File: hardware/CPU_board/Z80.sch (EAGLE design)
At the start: 46 parts, among them IC11 74HCT245DW, IC3 ATF16V8BP3, IC6 74AC273N, IC9 74HCT138N

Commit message: CPU board update
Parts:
- removed C11: 100n, rcl:C-EUC0805
- removed C15, C21, C6: 100n, rcl:C-EUC1206
- added JP3: (no value), pinhead:PINHD-1X2
- added R14: 10k, rcl:R-EU_0204/7
- IC3: value ATF16V8BP3 -> (none); device atmel:ATF16V8BP3 -> pal:16V8
- R1, R8: device rcl:R-EU_0207/12 -> rcl:R-EU_0204/7
- R10: device rcl:R-EU_0204/7 -> rcl:R-EU_R0603
- R4: device rcl:R-EU_R1206 -> rcl:R-EU_R0603
- R9: device rcl:R-EU_0204/7 -> rcl:R-EU_0207/10
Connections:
- removed net CF_DELAYED_RD: CON1G$1./IORD
- removed net CF_DELAYED_WR: CON1G$1./IOWR
- removed net CS_1: IC9A.Y1, SV2.58
- net !IORQ: now also IC3G$1.I6; no longer IC3.I3
- net !MREQ: now also IC3G$1.I3; no longer IC3.CLK
- net !RESET: now also R14.1
- net A15: now also IC3G$1.I4; no longer IC3.I2
- net A4: now also IC3G$1.I1; no longer IC3.I6
- net CF_CS0: now also IC3G$1.O5
- net CLK: now also IC3G$1.CLK
- net CS_EPROM: now also IC3G$1.O1; no longer IC3.O3
- net CS_RAM1: now also IC3G$1.O7; no longer IC3.O1
- net CS_RAM2: now also IC3G$1.O6; no longer IC3.O2
- net DMA_CS: now also IC9A.Y1; no longer IC3.O6
- net GND: now also JP3.2, SV2.58; no longer C11.2, C15.2, C21.2, C6.2, IC3.GND
- net INTA: now also IC3G$1.O0; no longer IC3.O4
- net LOCAL_IO_CS: now also IC3G$1.I7; no longer IC3.I5
- net M1: now also IC3G$1.I0; no longer IC3.I4
- net PORT_CS: now also IC3G$1.O3; no longer IC3.O5
- net RD: now also CON1G$1./IORD
- net ROM_SHADOW: now also IC3G$1.I5; no longer IC3.I1
- net VCC: now also JP3.1, R14.2; no longer C11.1, C15.1, C21.1, C6.1, IC3.VCC
- net WR: now also CON1G$1./IOWR, IC3G$1.I2
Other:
- moved on the sheet: C12, C13, C14, C18, C22, C7, C9, IC1, R2, R3, R4, R5

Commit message: CPU board update
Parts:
- added C4: 100n, rcl:C-EUC0603
- added D1: 1N4148DO35-7, diode:1N4148DO35-7
- added JP1: (no value), pinhead:PINHD-1X2
- added R15: (no value), rcl:R-EU_R0603
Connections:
- new net N$2: JP1.2, R15.1
- net !RESET: now also C4.1, D1.A, R15.2
- net GND: now also C4.2, JP1.1
- net VCC: now also D1.C
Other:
- moved on the sheet: R14

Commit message: bugs in CPU board design fixed
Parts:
- removed R9: 10k, rcl:R-EU_0207/10
- added R16: (no value), rcl:R-EU_0204/5
- added R17: (no value), rcl:R-EU_R0603
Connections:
- removed net N$20: IC9A.G1, R9.1
- new net N$3: IC2.IEI, R16.1
- net M1: now also IC9A.G1
- net VCC: now also R16.2, R17.2; no longer R9.2
- net WAIT: now also R17.1
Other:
- moved on the sheet: IC1, R2, R3, R4, R5

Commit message: CPU board and I/O board update
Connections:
- net !IORQ: now also SV2.44
- net M1: now also SV2.43
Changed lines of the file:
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@@
 <pinref part="SV2" gate="1" pin="1"/>
 <wire x1="160.02" y1="-71.12" x2="165.1" y2="-71.12" width="0.1524" layer="91"/>
+<label x="165.1" y="-71.12" size="1.4224" layer="95" xref="yes"/>
 </segment>
 </net>
@@
 <label x="43.18" y="-109.22" size="1.4224" layer="95" rot="R180" xref="yes"/>
 </segment>
+<segment>
+<pinref part="SV2" gate="1" pin="44"/>
+<wire x1="144.78" y1="-17.78" x2="139.7" y2="-17.78" width="0.1524" layer="91"/>
+<label x="139.7" y="-17.78" size="1.4224" layer="95" rot="R180" xref="yes"/>
+</segment>
 </net>
 <net name="!MREQ" class="0">
@@
 <label x="114.3" y="-144.78" size="1.4224" layer="95" rot="R180" xref="yes"/>
 </segment>
-</net>
+<segment>
+<pinref part="SV2" gate="1" pin="43"/>
+<wire x1="160.02" y1="-17.78" x2="165.1" y2="-17.78" width="0.1524" layer="91"/>
+<label x="165.1" y="-17.78" size="1.4224" layer="95" xref="yes"/>
+</segment>
+</net>

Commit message: CPU and I/O board update
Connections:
- removed net 8275_DACK: SV2.2
- removed net RDYIN: SV2.1
- new net IEO: IC2.IEO, SV2.2
- net INT: now also IC2.INT/PLSE
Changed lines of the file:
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@@
 <junction x="-17.78" y="30.48"/>
+</segment>
+<segment>
+<pinref part="IC2" gate="G$1" pin="INT/PLSE"/>
+<wire x1="-88.9" y1="12.7" x2="-93.98" y2="12.7" width="0.1524" layer="91"/>
 </segment>
 </net>
@@
 </segment>
 </net>
-<net name="RDYIN" class="0">
-<segment>
-<pinref part="SV2" gate="1" pin="1"/>
-<wire x1="160.02" y1="-71.12" x2="165.1" y2="-71.12" width="0.1524" layer="91"/>
-<label x="165.1" y="-71.12" size="1.4224" layer="95" xref="yes"/>
-</segment>
-</net>
 <net name="!RESET" class="0">
 <segment>
@@
 </segment>
 </net>
-<net name="8275_DACK" class="0">
-<segment>
-<pinref part="SV2" gate="1" pin="2"/>
-<wire x1="144.78" y1="-71.12" x2="139.7" y2="-71.12" width="0.1524" layer="91"/>
-<label x="139.7" y="-71.12" size="1.4224" layer="95" rot="R180" xref="yes"/>
-</segment>
-</net>
 <net name="!IORQ" class="0">
 <segment>
@@
 </segment>
 </net>
+<net name="IEO" class="0">
+<segment>
+<pinref part="SV2" gate="1" pin="2"/>
+<wire x1="144.78" y1="-71.12" x2="139.7" y2="-71.12" width="0.1524" layer="91"/>
+<label x="139.7" y="-71.12" size="1.778" layer="95" rot="R180" xref="yes"/>
+</segment>
+<segment>
+<pinref part="IC2" gate="G$1" pin="IEO"/>
+<wire x1="-88.9" y1="7.62" x2="-93.98" y2="7.62" width="0.1524" layer="91"/>
+</segment>
+</net>

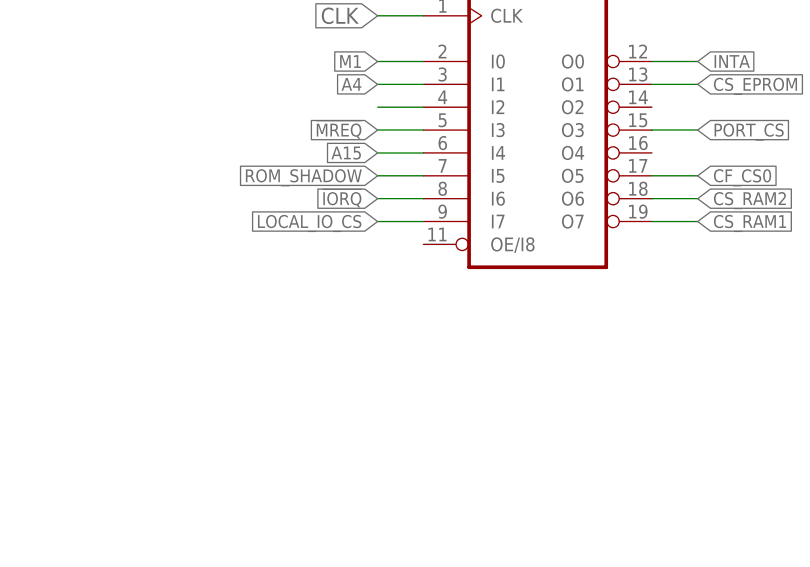
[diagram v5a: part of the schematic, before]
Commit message: Bug in CPU board fixed
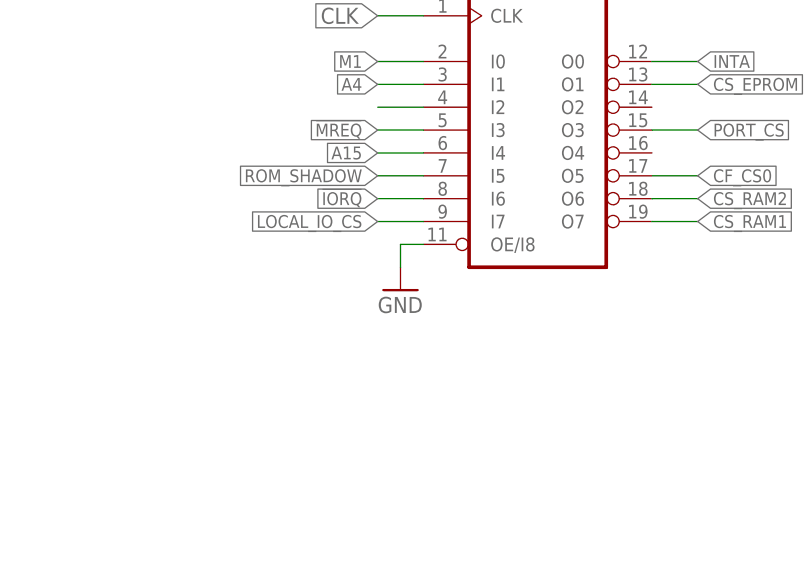
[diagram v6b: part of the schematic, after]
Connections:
- net GND: now also IC3G$1.OE/I8
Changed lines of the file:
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@@
 <part name="R16" library="rcl" deviceset="R-EU_" device="0204/5"/>
 <part name="R17" library="rcl" deviceset="R-EU_" device="R0603"/>
+<part name="GND10" library="supply1" deviceset="GND" device=""/>
 </parts>
 <sheets>
@@
 <instance part="R16" gate="G$1" x="-111.76" y="25.4" rot="R90"/>
 <instance part="R17" gate="G$1" x="2.54" y="43.18" rot="R90"/>
+<instance part="GND10" gate="1" x="45.72" y="-119.38"/>
 </instances>
 <busses>
@@
 <pinref part="GND9" gate="1" pin="GND"/>
 </segment>
+<segment>
+<pinref part="IC3" gate="G$1" pin="OE/I8"/>
+<pinref part="GND10" gate="1" pin="GND"/>
+<wire x1="48.26" y1="-114.3" x2="45.72" y2="-114.3" width="0.1524" layer="91"/>
+<wire x1="45.72" y1="-114.3" x2="45.72" y2="-116.84" width="0.1524" layer="91"/>
+</segment>
 </net>
